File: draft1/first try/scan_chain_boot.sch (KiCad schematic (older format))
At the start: 5 parts

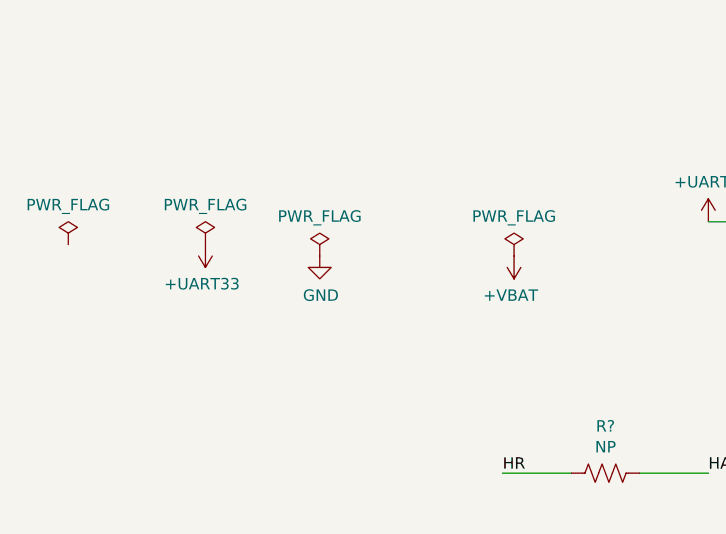
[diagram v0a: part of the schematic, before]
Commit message: added power flags
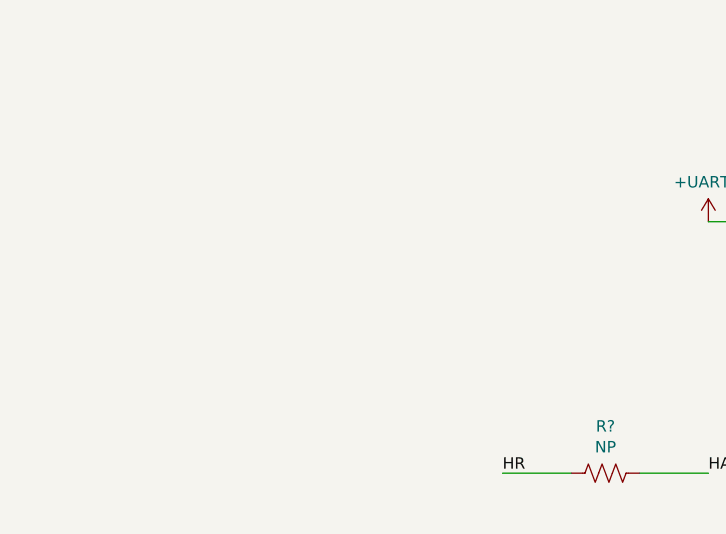
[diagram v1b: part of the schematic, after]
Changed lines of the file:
@@
 $Descr A4 11693 8268
 encoding utf-8
-Sheet 3 3
+Sheet 3 4
 Title ""
 Date ""
@@
 U 1 1 5F3DDAE9
 P 2900 4550
+AR Path="/5F3DDAE9" Ref="IC?"  Part="1"
+AR Path="/5F3B0B28/5F3DDAE9" Ref="IC?"  Part="1"
 F 0 "IC?" H 3550 4815 50  0000 C CNN
 F 1 "74AVC4TD245PW,118" H 3550 4724 50  0000 C CNN
@@
 U 1 1 5F3DDAF7
 P 6850 4500
+AR Path="/5F3DDAF7" Ref="IC?"  Part="1"
+AR Path="/5F3B0B28/5F3DDAF7" Ref="IC?"  Part="1"
 F 0 "IC?" H 7500 4765 50  0000 C CNN
 F 1 "74AVC4TD245PW,118" H 7500 4674 50  0000 C CNN
@@
 U 1 1 5F3DDAFD
 P 4200 5250
+AR Path="/5F3DDAFD" Ref="#PWR?"  Part="1"
+AR Path="/5F3B0B28/5F3DDAFD" Ref="#PWR?"  Part="1"
 F 0 "#PWR?" H 4200 5000 50  0001 C CNN
 F 1 "GND" H 4205 5077 50  0000 C CNN
@@
 U 1 1 5F3DDB03
 P 2900 5250
+AR Path="/5F3DDB03" Ref="#PWR?"  Part="1"
+AR Path="/5F3B0B28/5F3DDB03" Ref="#PWR?"  Part="1"
 F 0 "#PWR?" H 2900 5000 50  0001 C CNN
 F 1 "GND" H 2905 5077 50  0000 C CNN
@@
 U 1 1 5F3DDB09
 P 4200 5150
+AR Path="/5F3DDB09" Ref="#PWR?"  Part="1"
+AR Path="/5F3B0B28/5F3DDB09" Ref="#PWR?"  Part="1"
 F 0 "#PWR?" H 4200 4900 50  0001 C CNN
 F 1 "GND" V 4205 5022 50  0000 R CNN
@@
 U 1 1 5F3DDB0F
 P 2900 5150
+AR Path="/5F3DDB0F" Ref="#PWR?"  Part="1"
+AR Path="/5F3B0B28/5F3DDB0F" Ref="#PWR?"  Part="1"
 F 0 "#PWR?" H 2900 4900 50  0001 C CNN
 F 1 "GND" V 2905 5022 50  0000 R CNN
@@
 U 1 1 5F3DDB15
 P 4200 4650
+AR Path="/5F3DDB15" Ref="#PWR?"  Part="1"
+AR Path="/5F3B0B28/5F3DDB15" Ref="#PWR?"  Part="1"
 F 0 "#PWR?" H 4200 4400 50  0001 C CNN
 F 1 "GND" V 4205 4522 50  0000 R CNN
@@
 U 1 1 5F3DDB1B
 P 6850 5200
+AR Path="/5F3DDB1B" Ref="#PWR?"  Part="1"
+AR Path="/5F3B0B28/5F3DDB1B" Ref="#PWR?"  Part="1"
 F 0 "#PWR?" H 6850 4950 50  0001 C CNN
 F 1 "GND" H 6855 5027 50  0000 C CNN
@@
 U 1 1 5F3DDB21
 P 6850 5100
+AR Path="/5F3DDB21" Ref="#PWR?"  Part="1"
+AR Path="/5F3B0B28/5F3DDB21" Ref="#PWR?"  Part="1"
 F 0 "#PWR?" H 6850 4850 50  0001 C CNN
 F 1 "GND" V 6855 4972 50  0000 R CNN
@@
 U 1 1 5F3DDB27
 P 8150 5200
+AR Path="/5F3DDB27" Ref="#PWR?"  Part="1"
+AR Path="/5F3B0B28/5F3DDB27" Ref="#PWR?"  Part="1"
 F 0 "#PWR?" H 8150 4950 50  0001 C CNN
 F 1 "GND" H 8155 5027 50  0000 C CNN
@@
 U 1 1 5F3DDB2D
 P 6850 4600
+AR Path="/5F3DDB2D" Ref="#PWR?"  Part="1"
+AR Path="/5F3B0B28/5F3DDB2D" Ref="#PWR?"  Part="1"
 F 0 "#PWR?" H 6850 4350 50  0001 C CNN
 F 1 "GND" V 6855 4472 50  0000 R CNN
@@
 U 1 1 5F3DDB33
 P 8150 4600
+AR Path="/5F3DDB33" Ref="#PWR?"  Part="1"
+AR Path="/5F3B0B28/5F3DDB33" Ref="#PWR?"  Part="1"
 F 0 "#PWR?" H 8150 4350 50  0001 C CNN
 F 1 "GND" V 8155 4472 50  0000 R CNN
@@
 U 1 1 5F3DDB39
 P 8150 5100
+AR Path="/5F3DDB39" Ref="#PWR?"  Part="1"
+AR Path="/5F3B0B28/5F3DDB39" Ref="#PWR?"  Part="1"
 F 0 "#PWR?" H 8150 4850 50  0001 C CNN
 F 1 "GND" V 8155 4972 50  0000 R CNN
@@
 U 1 1 5F3DDB3F
 P 2900 4550
+AR Path="/5F3DDB3F" Ref="#PWR?"  Part="1"
+AR Path="/5F3B0B28/5F3DDB3F" Ref="#PWR?"  Part="1"
 F 0 "#PWR?" H 2900 4400 50  0001 C CNN
 F 1 "+VBAT" H 2915 4723 50  0000 C CNN
@@
 U 1 1 5F3DDB45
 P 2900 4650
+AR Path="/5F3DDB45" Ref="#PWR?"  Part="1"
+AR Path="/5F3B0B28/5F3DDB45" Ref="#PWR?"  Part="1"
 F 0 "#PWR?" H 2900 4500 50  0001 C CNN
 F 1 "+VBAT" V 2915 4778 50  0000 L CNN
@@
 U 1 1 5F3DDB4B
 P 6850 4500
+AR Path="/5F3DDB4B" Ref="#PWR?"  Part="1"
+AR Path="/5F3B0B28/5F3DDB4B" Ref="#PWR?"  Part="1"
 F 0 "#PWR?" H 6850 4350 50  0001 C CNN
 F 1 "+VBAT" H 6865 4673 50  0000 C CNN
@@
 U 1 1 5F3DDB6B
 P 10050 2450
+AR Path="/5F3DDB6B" Ref="J?"  Part="1"
+AR Path="/5F3B0B28/5F3DDB6B" Ref="J?"  Part="1"
 F 0 "J?" V 10267 2396 50  0000 C CNN
 F 1 "Conn_01x24" V 10176 2396 50  0000 C CNN
@@
 Wire Wire Line
 	9850 3150 9600 3150
-$Comp
-L power:PWR_FLAG #FLG?
-U 1 1 5F3DDB8D
-P 2800 2300
-F 0 "#FLG?" H 2800 2375 50  0001 C CNN
-F 1 "PWR_FLAG" H 2800 2473 50  0000 C CNN
-F 2 "" H 2800 2300 50  0001 C CNN
-F 3 "~" H 2800 2300 50  0001 C CNN
-	1    2800 2300
-	1    0    0    -1
-$EndComp
-$Comp
-L power:PWR_FLAG #FLG?
-U 1 1 5F3DDB93
-P 3650 2300
-F 0 "#FLG?" H 3650 2375 50  0001 C CNN
-F 1 "PWR_FLAG" H 3650 2473 50  0000 C CNN
-F 2 "" H 3650 2300 50  0001 C CNN
-F 3 "~" H 3650 2300 50  0001 C CNN
-	1    3650 2300
-	1    0    0    -1
-$EndComp
-$Comp
-L power:GND #PWR?
-U 1 1 5F3DDB99
-P 2800 2300
-F 0 "#PWR?" H 2800 2050 50  0001 C CNN
-F 1 "GND" H 2805 2127 50  0000 C CNN
-F 2 "" H 2800 2300 50  0001 C CNN
-F 3 "" H 2800 2300 50  0001 C CNN
-	1    2800 2300
-	1    0    0    -1
-$EndComp
-$Comp
-L draft1library:+VBAT #PWR?
-U 1 1 5F3DDB9F
-P 3650 2300
-F 0 "#PWR?" H 3650 2150 50  0001 C CNN
-F 1 "+VBAT" H 3665 2473 50  0000 C CNN
-F 2 "" H 3650 2300 50  0001 C CNN
-F 3 "" H 3650 2300 50  0001 C CNN
-	1    3650 2300
-	-1   0    0    1
-$EndComp
 Text GLabel 6450 4700 0    50   BiDi ~ 0
 LF_CLK_EXT_IN
@@
 U 1 1 5F3DDBB1
 P 9600 2750
+AR Path="/5F3DDBB1" Ref="#PWR?"  Part="1"
+AR Path="/5F3B0B28/5F3DDBB1" Ref="#PWR?"  Part="1"
 F 0 "#PWR?" H 9600 2500 50  0001 C CNN
 F 1 "GND" V 9605 2622 50  0000 R CNN
@@
 U 1 1 5F3DDBBA
 P 4050 3250
+AR Path="/5F3DDBBA" Ref="R?"  Part="1"
+AR Path="/5F3B0B28/5F3DDBBA" Ref="R?"  Part="1"
 F 0 "R?" V 3845 3250 50  0000 C CNN
 F 1 "NP" V 3936 3250 50  0000 C CNN
@@
 U 1 1 5F3DDBC0
 P 5000 2150
+AR Path="/5F3DDBC0" Ref="R?"  Part="1"
+AR Path="/5F3B0B28/5F3DDBC0" Ref="R?"  Part="1"
 F 0 "R?" V 4795 2150 50  0000 C CNN
 F 1 "100k" V 4886 2150 50  0000 C CNN
@@
 U 1 1 5F3DDBC6
 P 4600 4550
+AR Path="/5F3DDBC6" Ref="#PWR?"  Part="1"
+AR Path="/5F3B0B28/5F3DDBC6" Ref="#PWR?"  Part="1"
 F 0 "#PWR?" H 4600 4400 50  0001 C CNN
 F 1 "+UART33" H 4615 4723 50  0000 C CNN
@@
 U 1 1 5F3DDBCC
 P 8550 4500
+AR Path="/5F3DDBCC" Ref="#PWR?"  Part="1"
+AR Path="/5F3B0B28/5F3DDBCC" Ref="#PWR?"  Part="1"
 F 0 "#PWR?" H 8550 4350 50  0001 C CNN
 F 1 "+UART33" H 8565 4673 50  0000 C CNN
@@
 U 1 1 5F3DDBD9
 P 4500 2150
+AR Path="/5F3DDBD9" Ref="#PWR?"  Part="1"
+AR Path="/5F3B0B28/5F3DDBD9" Ref="#PWR?"  Part="1"
 F 0 "#PWR?" H 4500 2000 50  0001 C CNN
 F 1 "+UART33" H 4515 2323 50  0000 C CNN
@@
 	1    0    0    -1
 $EndComp
-$Comp
-L power:PWR_FLAG #FLG?
-U 1 1 5F3DDBDF
-P 2300 2250
-F 0 "#FLG?" H 2300 2325 50  0001 C CNN
-F 1 "PWR_FLAG" H 2300 2423 50  0000 C CNN
-F 2 "" H 2300 2250 50  0001 C CNN
-F 3 "~" H 2300 2250 50  0001 C CNN
-	1    2300 2250
-	1    0    0    -1
-$EndComp
-$Comp
-L draft1library:+UART33 #PWR?
-U 1 1 5F3DDBE5
-P 2300 2250
-F 0 "#PWR?" H 2300 2100 50  0001 C CNN
-F 1 "+UART33" H 2315 2423 50  0000 C CNN
-F 2 "" H 2300 2250 50  0001 C CNN
-F 3 "" H 2300 2250 50  0001 C CNN
-	1    2300 2250
-	-1   0    0    1
-$EndComp
-$Comp
-L power:PWR_FLAG #FLG?
-U 1 1 5F3DDBEB
-P 1700 2250
-F 0 "#FLG?" H 1700 2325 50  0001 C CNN
-F 1 "PWR_FLAG" H 1700 2423 50  0000 C CNN
-F 2 "" H 1700 2250 50  0001 C CNN
-F 3 "~" H 1700 2250 50  0001 C CNN
-	1    1700 2250
-	1    0    0    -1
-$EndComp
